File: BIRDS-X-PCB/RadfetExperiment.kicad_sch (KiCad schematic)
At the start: 37 parts, among them U301 VT03, U302 VT03, U303 VT03, U304 VT03, U305 TL974IPWR, U306 ADG734, U307 LM335DT, U308 LM334M, U309 LM334M, U310 LM334M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

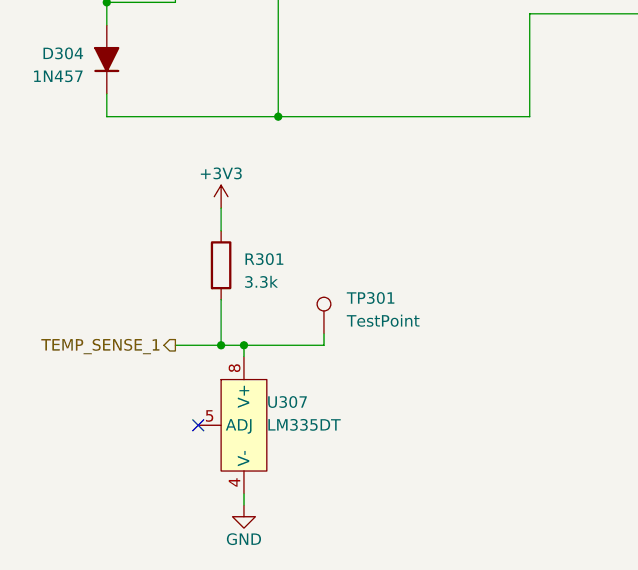
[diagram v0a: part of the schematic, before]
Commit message: Change temperature sensor
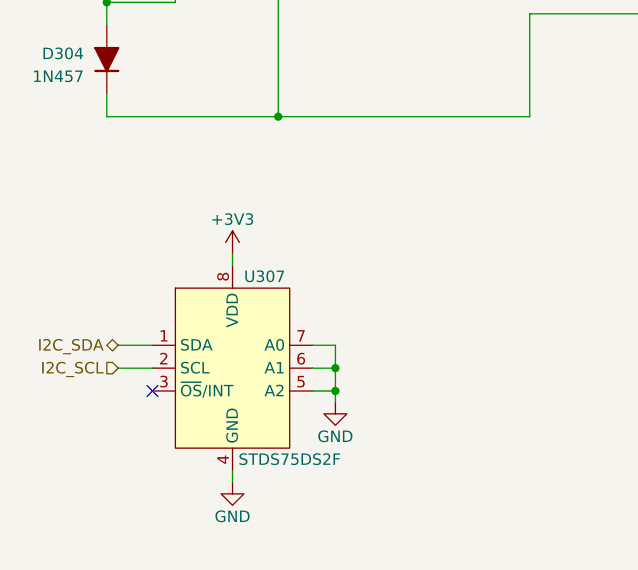
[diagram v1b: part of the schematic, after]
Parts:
- removed R301: 3.3k, Resistor_SMD:R_0603_1608Metric_Pad0.98x0.95mm_HandSolder, symbol Device:R
- removed TP301: TestPoint, TestPoint:TestPoint_Pad_D1.5mm, symbol Connector:TestPoint
- removed U307: LM335DT, Package_SO:SOIC-8_3.9x4.9mm_P1.27mm, symbol BIRDS-X_Symbols_Lib:LM335D
- added U307: STDS75DS2F, Package_SO:MSOP-8_3x3mm_P0.65mm, symbol Project-Supernova-Symbol-Lib:STDS75DS2F
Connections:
- net +3V3: now also U307.8 (VDD)
- net GND: now also U307.4 (GND), U307.5 (A2), U307.6 (A1), U307.7 (A0)
- new net I2C_SCL: U307.2 (SCL)
- new net I2C_SDA: U307.1 (SDA)

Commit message: Tweaks
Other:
- note removed: "TODO add mounting holes"
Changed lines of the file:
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@@
-    (effects (font (size 1.27 1.27)) (justify left bottom))
-  )
-  (text "TODO add mounting holes" (at 101.6 182.88 0)
     (effects (font (size 1.27 1.27)) (justify left bottom))
   )

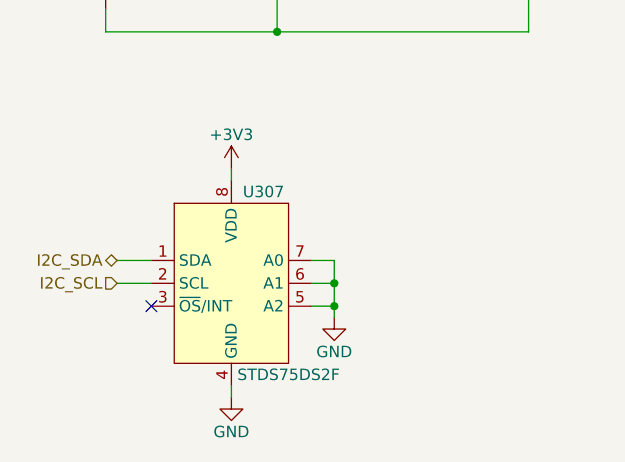
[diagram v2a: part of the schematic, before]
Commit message: Schematic updates
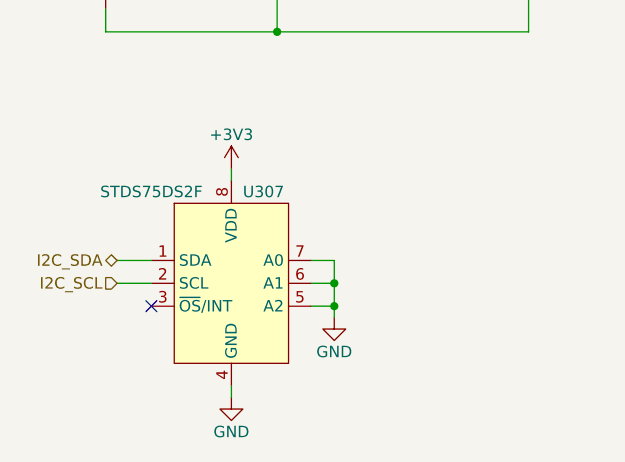
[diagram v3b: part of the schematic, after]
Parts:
- U307: symbol Project-Supernova-Symbol-Lib:STDS75DS2F -> BIRDS-X_Symbols_Lib:STDS75DS2F
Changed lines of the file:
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@@
     )
   )
-  (symbol (lib_id "Project-Supernova-Symbol-Lib:STDS75DS2F") (at 36.83 181.61 0) (unit 1)
+  (symbol (lib_id "BIRDS-X_Symbols_Lib:STDS75DS2F") (at 36.83 181.61 0) (unit 1)
     (in_bom yes) (on_board yes) (dnp no)
     (property "Reference" "U307" (at 38.1 171.45 0)
       (effects (font (size 1.27 1.27)) (justify left))
     )
-    (property "Value" "STDS75DS2F" (at 43.18 191.77 0)
+    (property "Value" "STDS75DS2F" (at 27.94 171.45 0)
       (effects (font (size 1.27 1.27)))
     )

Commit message: Major layout
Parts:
- removed U307: STDS75DS2F, Package_SO:MSOP-8_3x3mm_P0.65mm, symbol BIRDS-X_Symbols_Lib:STDS75DS2F
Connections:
- no-connect marks 1 -> 0
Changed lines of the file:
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@@
   (junction (at 115.57 31.75) (diameter 0) (color 0 0 0 0)
   )
-  (junction (at 48.26 181.61) (diameter 0) (color 0 0 0 0)
-  )
   (junction (at 195.58 62.23) (diameter 0) (color 0 0 0 0)
   )
@@
   (junction (at 25.4 102.87) (diameter 0) (color 0 0 0 0)
   )
-  (junction (at 48.26 184.15) (diameter 0) (color 0 0 0 0)
-  )
   (junction (at 118.11 97.79) (diameter 0) (color 0 0 0 0)
   )
@@
   (junction (at 209.55 151.13) (diameter 0) (color 0 0 0 0)
   )
-  (no_connect (at 27.94 184.15))
   (wire (pts (xy 161.29 59.69) (xy 179.07 59.69))
     (stroke (width 0) (type default))
   )
-  (wire (pts (xy 24.13 181.61) (xy 27.94 181.61))
-    (stroke (width 0) (type default))
-  )
   (wire (pts (xy 54.61 53.34) (xy 54.61 59.69))
     (stroke (width 0) (type default))
@@
     (stroke (width 0) (type default))
   )
-  (wire (pts (xy 48.26 179.07) (xy 48.26 181.61))
-    (stroke (width 0) (type default))
-  )
   (wire (pts (xy 157.48 52.07) (xy 157.48 59.69))
     (stroke (width 0) (type default))
@@
     (stroke (width 0) (type default))
   )
-  (wire (pts (xy 36.83 193.04) (xy 36.83 194.31))
-    (stroke (width 0) (type default))
-  )
   (wire (pts (xy 69.85 59.69) (xy 91.44 59.69))
     (stroke (width 0) (type default))
@@
     (stroke (width 0) (type default))
   )
-  (wire (pts (xy 36.83 168.91) (xy 36.83 170.18))
-    (stroke (width 0) (type default))
-  )
   (wire (pts (xy 123.19 134.62) (xy 157.48 134.62))
     (stroke (width 0) (type default))
@@
     (stroke (width 0) (type default))
   )
-  (wire (pts (xy 45.72 181.61) (xy 48.26 181.61))
-    (stroke (width 0) (type default))
-  )
   (wire (pts (xy 31.75 62.23) (xy 31.75 60.96))
     (stroke (width 0) (type default))
@@
     (stroke (width 0) (type default))
   )
-  (wire (pts (xy 24.13 179.07) (xy 27.94 179.07))
-    (stroke (width 0) (type default))
-  )
   (wire (pts (xy 195.58 142.24) (xy 209.55 142.24))
     (stroke (width 0) (type default))
@@
     (stroke (width 0) (type default))
   )
-  (wire (pts (xy 45.72 179.07) (xy 48.26 179.07))
-    (stroke (width 0) (type default))
-  )
   (wire (pts (xy 118.11 91.44) (xy 125.73 91.44))
     (stroke (width 0) (type default))
@@
     (stroke (width 0) (type default))
   )
-  (wire (pts (xy 48.26 184.15) (xy 45.72 184.15))
-    (stroke (width 0) (type default))
-  )
   (wire (pts (xy 209.55 151.13) (xy 212.09 151.13))
     (stroke (width 0) (type default))
@@
   )
   (wire (pts (xy 82.55 27.94) (xy 82.55 31.75))
-    (stroke (width 0) (type default))
-  )
-  (wire (pts (xy 48.26 185.42) (xy 48.26 184.15))
-    (stroke (width 0) (type default))
-  )
-  (wire (pts (xy 48.26 181.61) (xy 48.26 184.15))
     (stroke (width 0) (type default))
   )
@@
     (effects (font (size 1.27 1.27)) (justify right))
   )
-  (hierarchical_label "I2C_SDA" (shape bidirectional) (at 24.13 179.07 180) (fields_autoplaced)
-    (effects (font (size 1.27 1.27)) (justify right))
-  )
   (hierarchical_label "RFET_EN" (shape input) (at 92.71 48.26 180) (fields_autoplaced)
     (effects (font (size 1.27 1.27)) (justify right))
@@
     (effects (font (size 1.27 1.27)) (justify left))
   )
-  (hierarchical_label "I2C_SCL" (shape input) (at 24.13 181.61 180) (fields_autoplaced)
-    (effects (font (size 1.27 1.27)) (justify right))
-  )
   (hierarchical_label "RFET_SENSE_3" (shape output) (at 212.09 121.92 0) (fields_autoplaced)
     (effects (font (size 1.27 1.27)) (justify left))
@@
         (path "/c2796b15-795a-4d6e-ad4b-0ba87ded4bc9/adc73a10-1d27-484e-8ce9-d638694b8e29"
           (reference "R312") (unit 1)
-        )
-      )
-    )
-  )
-  (symbol (lib_id "power:GND") (at 48.26 185.42 0) (unit 1)
-    (in_bom yes) (on_board yes) (dnp no)
-    (property "Reference" "#PWR04" (at 48.26 191.77 0)
-      (effects (font (size 1.27 1.27)) hide)
-    )
-    (property "Value" "GND" (at 48.26 189.23 0)
-      (effects (font (size 1.27 1.27)))
-    )
-    (property "Footprint" "" (at 48.26 185.42 0)
-      (effects (font (size 1.27 1.27)) hide)
-    )
-    (property "Datasheet" "" (at 48.26 185.42 0)
-      (effects (font (size 1.27 1.27)) hide)
-    )
-    (pin "1")
-    (instances
-      (project "RFM95-Multi-PCB"
-        (path "/85ef8898-68b3-4189-afc2-72beb189ca0c"
-          (reference "#PWR04") (unit 1)
-        )
-      )
-      (project "BIRDS-X-PCB"
-        (path "/c2796b15-795a-4d6e-ad4b-0ba87ded4bc9/adc73a10-1d27-484e-8ce9-d638694b8e29"
-          (reference "#PWR0307") (unit 1)
-        )
-      )
-      (project "Project-Supernova-PCB"
-        (path "/c3359c04-e049-4b5c-b9e7-2425ad933569"
-          (reference "#PWR019") (unit 1)
         )
       )
@@
     )
   )
-  (symbol (lib_id "power:GND") (at 36.83 194.31 0) (unit 1)
-    (in_bom yes) (on_board yes) (dnp no)
-    (property "Reference" "#PWR04" (at 36.83 200.66 0)
-      (effects (font (size 1.27 1.27)) hide)
-    )
-    (property "Value" "GND" (at 36.83 198.12 0)
-      (effects (font (size 1.27 1.27)))
-    )
-    (property "Footprint" "" (at 36.83 194.31 0)
-      (effects (font (size 1.27 1.27)) hide)
-    )
-    (property "Datasheet" "" (at 36.83 194.31 0)
-      (effects (font (size 1.27 1.27)) hide)
-    )
-    (pin "1")
-    (instances
-      (project "RFM95-Multi-PCB"
-        (path "/85ef8898-68b3-4189-afc2-72beb189ca0c"
-          (reference "#PWR04") (unit 1)
-        )
-      )
-      (project "BIRDS-X-PCB"
-        (path "/c2796b15-795a-4d6e-ad4b-0ba87ded4bc9/adc73a10-1d27-484e-8ce9-d638694b8e29"
-          (reference "#PWR0306") (unit 1)
-        )
-      )
-      (project "Project-Supernova-PCB"
-        (path "/c3359c04-e049-4b5c-b9e7-2425ad933569"
-          (reference "#PWR020") (unit 1)
-        )
-      )
-    )
-  )
   (symbol (lib_id "Device:R_US") (at 209.55 116.84 0) (unit 1)
     (in_bom yes) (on_board yes) (dnp no) (fields_autoplaced)
@@
     )
   )
-  (symbol (lib_id "power:+3V3") (at 36.83 168.91 0) (unit 1)
-    (in_bom yes) (on_board yes) (dnp no) (fields_autoplaced)
-    (property "Reference" "#PWR0305" (at 36.83 172.72 0)
-      (effects (font (size 1.27 1.27)) hide)
-    )
-    (property "Value" "+3V3" (at 36.83 165.1 0)
-      (effects (font (size 1.27 1.27)))
-    )
-    (property "Footprint" "" (at 36.83 168.91 0)
-      (effects (font (size 1.27 1.27)) hide)
-    )
-    (property "Datasheet" "" (at 36.83 168.91 0)
-      (effects (font (size 1.27 1.27)) hide)
-    )
-    (pin "1")
-    (instances
-      (project "BIRDS-X-PCB"
-        (path "/c2796b15-795a-4d6e-ad4b-0ba87ded4bc9/adc73a10-1d27-484e-8ce9-d638694b8e29"
-          (reference "#PWR0305") (unit 1)
-        )
-      )
-      (project "Project-Supernova-PCB"
-        (path "/c3359c04-e049-4b5c-b9e7-2425ad933569"
-          (reference "#PWR046") (unit 1)
-        )
-      )
-    )
-  )
   (symbol (lib_id "BIRDS-X_Symbols_Lib:1N457") (at 25.4 109.22 90) (mirror x) (unit 1)
     (in_bom yes) (on_board yes) (dnp no)
@@
         )
       )
-    )
-  )
-  (symbol (lib_id "BIRDS-X_Symbols_Lib:STDS75DS2F") (at 36.83 181.61 0) (unit 1)
-    (in_bom yes) (on_board yes) (dnp no)
-    (property "Reference" "U307" (at 38.1 171.45 0)
-      (effects (font (size 1.27 1.27)) (justify left))
-    )
-    (property "Value" "STDS75DS2F" (at 27.94 171.45 0)
-      (effects (font (size 1.27 1.27)))
-    )
-    (property "Footprint" "Package_SO:MSOP-8_3x3mm_P0.65mm" (at 36.83 203.2 0)
-      (effects (font (size 1.27 1.27)) hide)
-    )
-    (property "Datasheet" "https://datasheet.lcsc.com/lcsc/1810231426_STMicroelectronics-STDS75DS2F_C283289.pdf" (at 36.83 205.74 0)
-      (effects (font (size 1.27 1.27)) hide)
-    )
-    (property "LCSC" "C283289" (at 43.18 200.66 0)
-      (effects (font (size 1.27 1.27)) hide)
-    )
-    (pin "1")
-    (pin "2")
-    (pin "3")
-    (pin "4")
-    (pin "5")
-    (pin "6")
-    (pin "7")
-    (pin "8")
-    (instances
-      (project "BIRDS-X-PCB"
-        (path "/c2796b15-795a-4d6e-ad4b-0ba87ded4bc9/adc73a10-1d27-484e-8ce9-d638694b8e29"
-          (reference "U307") (unit 1)
-        )
-      )
-      (project "Project-Supernova-PCB"
-        (path "/c3359c04-e049-4b5c-b9e7-2425ad933569"
-          (reference "U4") (unit 1)
-        )
-      )

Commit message: Finish PCB layout
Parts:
- JP301: footprint Connector_PinHeader_2.54mm:PinHeader_1x02_P2.54mm_Vertical -> Connector_PinHeader_1.27mm:PinHeader_1x02_P1.27mm_Vertical
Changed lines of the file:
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@@
       (effects (font (size 1.27 1.27)) hide)
     )
-    (property "Footprint" "Connector_PinHeader_2.54mm:PinHeader_1x02_P2.54mm_Vertical" (at 64.77 59.69 0)
+    (property "Footprint" "Connector_PinHeader_1.27mm:PinHeader_1x02_P1.27mm_Vertical" (at 64.77 59.69 0)
       (effects (font (size 1.27 1.27)) hide)
     )
